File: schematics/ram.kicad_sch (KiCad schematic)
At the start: 5 parts, among them J2 myBus, U2 71256SA, U3 4NAND

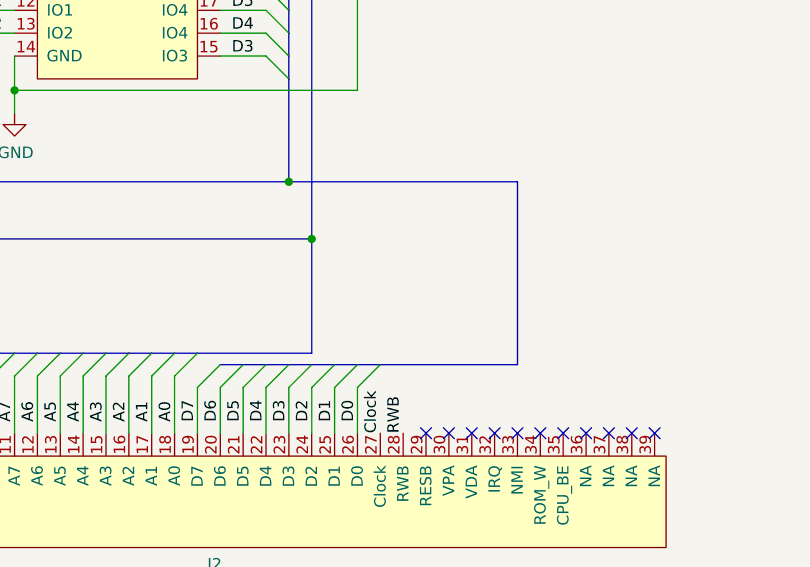
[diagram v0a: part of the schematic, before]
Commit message: Fix errors in schematics
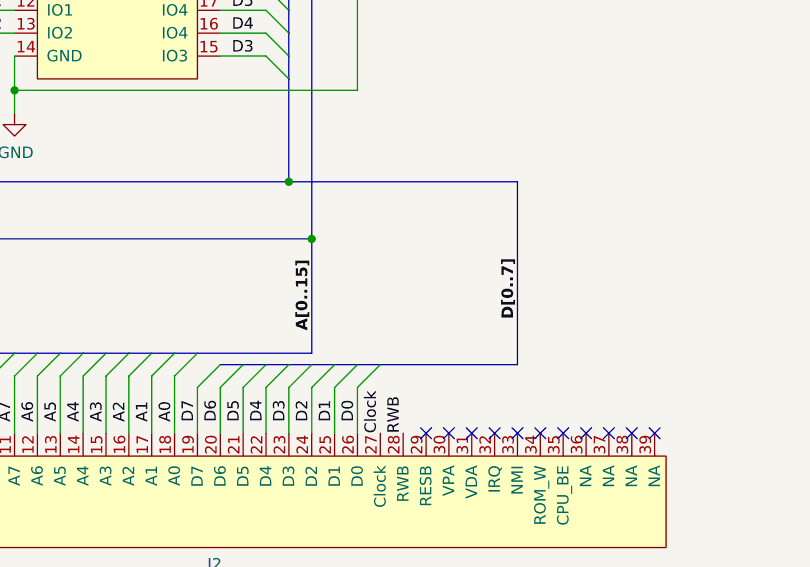
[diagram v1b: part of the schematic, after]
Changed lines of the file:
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@@
+		)
+	)
+	(label "A[0..15]"
+		(at 110.49 121.92 90)
+		(fields_autoplaced yes)
+		(effects
+			(font
+				(size 1.27 1.27)
+				(bold yes)
+			)
+			(justify left bottom)
 		)
 	)
@@
 			)
 			(justify left bottom)
+		)
+	)
+	(label "D[0..7]"
+		(at 133.35 120.65 90)
+		(fields_autoplaced yes)
+		(effects
+			(font
+				(size 1.27 1.27)
+				(bold yes)
+			)
+			(justify left bottom)

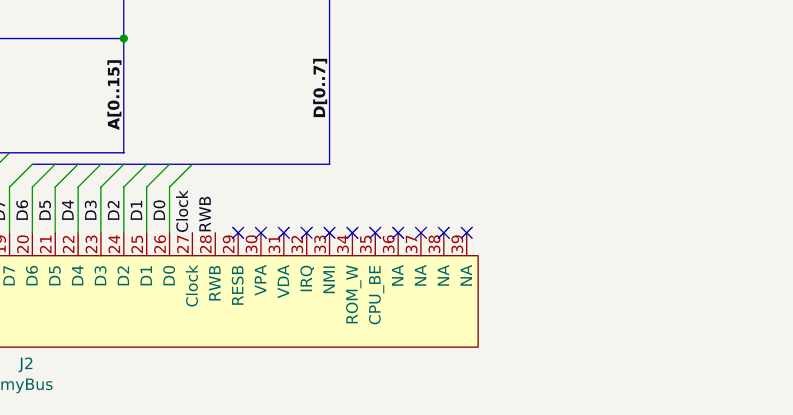
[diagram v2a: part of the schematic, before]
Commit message: Update ROM design
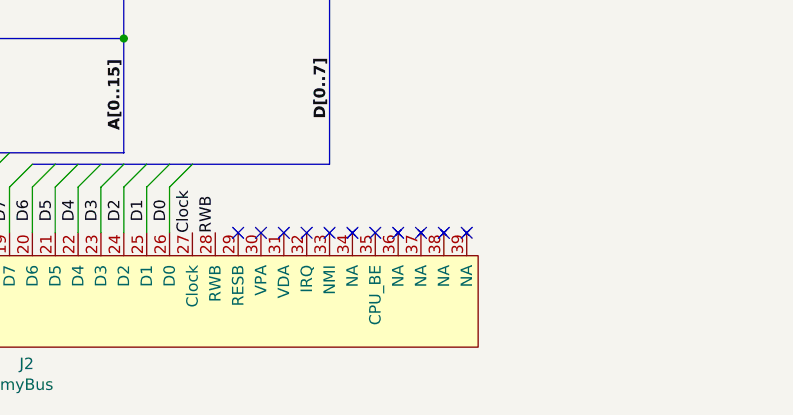
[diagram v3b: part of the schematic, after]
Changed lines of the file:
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@@
 	(label "RWB"
 		(at 100.33 60.96 0)
-		(fields_autoplaced yes)
 		(effects
 			(font
@@
 	(label "A10"
 		(at 69.85 132.08 90)
-		(fields_autoplaced yes)
 		(effects
 			(font
@@
 	(label "A7"
 		(at 77.47 132.08 90)
-		(fields_autoplaced yes)
 		(effects
 			(font
@@
 	(label "A4"
 		(at 85.09 132.08 90)
-		(fields_autoplaced yes)
 		(effects
 			(font
@@
 	(label "A10"
 		(at 102.87 76.2 0)
-		(fields_autoplaced yes)
 		(effects
 			(font
@@
 	(label "A9"
 		(at 72.39 132.08 90)
-		(fields_autoplaced yes)
 		(effects
 			(font
@@
 	(label "A7"
 		(at 72.39 63.5 0)
-		(fields_autoplaced yes)
 		(effects
 			(font
@@
 	(label "A5"
 		(at 72.39 68.58 0)
-		(fields_autoplaced yes)
 		(effects
 			(font
@@
 	(label "A6"
 		(at 72.39 66.04 0)
-		(fields_autoplaced yes)
 		(effects
 			(font
@@
 	(label "A14"
 		(at 59.69 132.08 90)
-		(fields_autoplaced yes)
 		(effects
 			(font
@@
 	(label "A5"
 		(at 82.55 132.08 90)
-		(fields_autoplaced yes)
 		(effects
 			(font
@@
 	(label "A3"
 		(at 72.39 73.66 0)
-		(fields_autoplaced yes)
 		(effects
 			(font
@@
 	(label "D7"
 		(at 101.6 81.28 0)
-		(fields_autoplaced yes)
 		(effects
 			(font
@@
 	(label "D7"
 		(at 97.79 132.08 90)
-		(fields_autoplaced yes)
 		(effects
 			(font
@@
 	(label "D1"
 		(at 73.66 86.36 0)
-		(fields_autoplaced yes)
 		(effects
 			(font
@@
 	(label "A1"
 		(at 72.39 78.74 0)
-		(fields_autoplaced yes)
 		(effects
 			(font
@@
 	(label "D3"
 		(at 101.6 91.44 0)
-		(fields_autoplaced yes)
 		(effects
 			(font
@@
 	(label "A12"
 		(at 64.77 132.08 90)
-		(fields_autoplaced yes)
 		(effects
 			(font
@@
 	(label "A13"
 		(at 62.23 132.08 90)
-		(fields_autoplaced yes)
 		(effects
 			(font
@@
 	(label "Clock"
 		(at 121.92 68.58 180)
-		(fields_autoplaced yes)
 		(effects
 			(font
@@
 	(label "A6"
 		(at 80.01 132.08 90)
-		(fields_autoplaced yes)
 		(effects
 			(font
@@
 	(label "A3"
 		(at 87.63 132.08 90)
-		(fields_autoplaced yes)
 		(effects
 			(font
@@
 	(label "D5"
 		(at 102.87 132.08 90)
-		(fields_autoplaced yes)
 		(effects
 			(font
@@
 	(label "A15"
 		(at 121.92 58.42 180)
-		(fields_autoplaced yes)
 		(effects
 			(font
@@
 	(label "D4"
 		(at 105.41 132.08 90)
-		(fields_autoplaced yes)
 		(effects
 			(font
@@
 	(label "A1"
 		(at 92.71 132.08 90)
-		(fields_autoplaced yes)
 		(effects
 			(font
@@
 	(label "A11"
 		(at 102.87 71.12 0)
-		(fields_autoplaced yes)
 		(effects
 			(font
@@
 	(label "A2"
 		(at 72.39 76.2 0)
-		(fields_autoplaced yes)
 		(effects
 			(font
@@
 	(label "A13"
 		(at 102.87 63.5 0)
-		(fields_autoplaced yes)
 		(effects
 			(font
@@
 	(label "D0"
 		(at 73.66 83.82 0)
-		(fields_autoplaced yes)
 		(effects
 			(font
@@
 	(label "D2"
 		(at 110.49 132.08 90)
-		(fields_autoplaced yes)
 		(effects
 			(font
@@
 	(label "A8"
 		(at 74.93 132.08 90)
-		(fields_autoplaced yes)
 		(effects
 			(font
@@
 	(label "A4"
 		(at 72.39 71.12 0)
-		(fields_autoplaced yes)
 		(effects
 			(font
@@
 	(label "A14"
 		(at 72.39 58.42 0)
-		(fields_autoplaced yes)
 		(effects
 			(font
@@
 	(label "D5"
 		(at 101.6 86.36 0)
-		(fields_autoplaced yes)
 		(effects
 			(font
@@
 	(label "D2"
 		(at 73.66 88.9 0)
-		(fields_autoplaced yes)
 		(effects
 			(font
@@
 	(label "A0"
 		(at 95.25 132.08 90)
-		(fields_autoplaced yes)
 		(effects
 			(font
@@
 	(label "D3"
 		(at 107.95 132.08 90)
-		(fields_autoplaced yes)
 		(effects
 			(font
@@
 	(label "A0"
 		(at 72.39 81.28 0)
-		(fields_autoplaced yes)
 		(effects
 			(font
@@
 	(label "D1"
 		(at 113.03 132.08 90)
-		(fields_autoplaced yes)
 		(effects
 			(font
@@
 	(label "D0"
 		(at 115.57 132.08 90)
-		(fields_autoplaced yes)
 		(effects
 			(font
@@
 	(label "A[0..15]"
 		(at 110.49 121.92 90)
-		(fields_autoplaced yes)
 		(effects
 			(font
@@
 	(label "A12"
 		(at 72.39 60.96 0)
-		(fields_autoplaced yes)
 		(effects
 			(font
@@
 	(label "A8"
 		(at 102.87 66.04 0)
-		(fields_autoplaced yes)
 		(effects
 			(font
@@
 	(label "A11"
 		(at 67.31 132.08 90)
-		(fields_autoplaced yes)
 		(effects
 			(font
@@
 	(label "RWB"
 		(at 120.65 133.35 90)
-		(fields_autoplaced yes)
 		(effects
 			(font
@@
 	(label "D6"
 		(at 101.6 83.82 0)
-		(fields_autoplaced yes)
 		(effects
 			(font
@@
 	(label "D4"
 		(at 101.6 88.9 0)
-		(fields_autoplaced yes)
 		(effects
 			(font
@@
 	(label "D6"
 		(at 100.33 132.08 90)
-		(fields_autoplaced yes)
 		(effects
 			(font
@@
 	(label "A15"
 		(at 57.15 133.35 90)
-		(fields_autoplaced yes)
 		(effects
 			(font
@@
 	(label "A2"
 		(at 90.17 132.08 90)
-		(fields_autoplaced yes)
 		(effects
 			(font
@@
 	(label "Clock"
 		(at 118.11 133.35 90)
-		(fields_autoplaced yes)
 		(effects
 			(font
@@
 	(label "D[0..7]"
 		(at 133.35 120.65 90)
-		(fields_autoplaced yes)
 		(effects
 			(font
@@
 	(label "A9"
 		(at 102.87 68.58 0)
-		(fields_autoplaced yes)
-		(effects
-			(font
+		(effects
+			(font
